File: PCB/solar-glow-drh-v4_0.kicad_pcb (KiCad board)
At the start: 2 copper layers, 50.8 x 88.9 mm, 65 parts, among them J1 UPDI hdr, Q1 BCP5316MTWG, SW2 LED master, U1 AVR64DD28 (VQFN28), U2 ALD910025SALI, U3 ADXL367, U4 TLV3011BIDBVR, U5 NT3H2211, U6 TPS22918

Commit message: pcb(v4_0): stage AEM10300 island parts off-board, net-tagged for rewiring
Place the 13 new v4 harvest parts (U8 AEM10300, U9 LDO, L2, CSRC/CINT/CSTO,
C22-C24, R15-R17, FB1) off the right edge of the board (x>50.8, on B.Cu),
each pad net-tagged per v4-aem10300-prewiring.md section 2, so the ratsnest
guides placement during the rewire. Cloned from existing footprints to match
this board's name-only-net format: U8 from U1 (QFN-28 4x4 0.4mm, 2.65 mm EP
-- matches the AEM10300 land), U9 from U6 (SOT-23), passives from the 0402
land. Larger parts (L2 / CSRC / CINT / CSTO / FB1) are 0402 placeholders to
reland in KiCad.

Existing 65 footprints and all current routing are untouched; the supercap
2S2P pack is verified balanced (VS-[SC1||SC2]-MID-[SC3||SC4]-GND).

Not KiCad-validated (no kicad-cli / pcbnew in this env): open in KiCad to
confirm it loads before relying on it. Structure checked by paren-balance,
reparse (65->78 footprints), and UUID-uniqueness.

Co-Authored-By: Claude Opus 4.8 <noreply@anthropic.com>
Claude-Session: https://claude.ai/code/session_01PBK3zFENdvoGtn8yP7qPA8
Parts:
- added C22: 1uF, solarglow:C1, B.Cu at (57.0, 37.0)
- added C23: 1uF, solarglow:C1, B.Cu at (61.0, 37.0)
- added C24: 100nF, solarglow:C1, B.Cu at (65.0, 37.0)
- added CINT: 10uF *0603, solarglow:C1, B.Cu at (61.0, 32.0)
- added CSRC: 22uF *0805, solarglow:C1, B.Cu at (57.0, 32.0)
- added CSTO: 100uF *bulk, solarglow:C1, B.Cu at (65.0, 32.0)
- added FB1: ferrite *0603, solarglow:C1, B.Cu at (69.0, 37.0)
- added L2: 10uH *IND-land, solarglow:C1, B.Cu at (67.0, 26.0)
- added R15: 2M, solarglow:C1, B.Cu at (57.0, 42.0)
- added R16: 1M, solarglow:C1, B.Cu at (61.0, 42.0)
- added R17: 1M, solarglow:C1, B.Cu at (65.0, 42.0)
- added U8: AEM10300, solarglow:U1, B.Cu at (62.0, 16.0)
- added U9: TPS7A0233 (SOT23-5*), Package_TO_SOT_SMD:SOT-23-6, B.Cu at (58.0, 26.0)

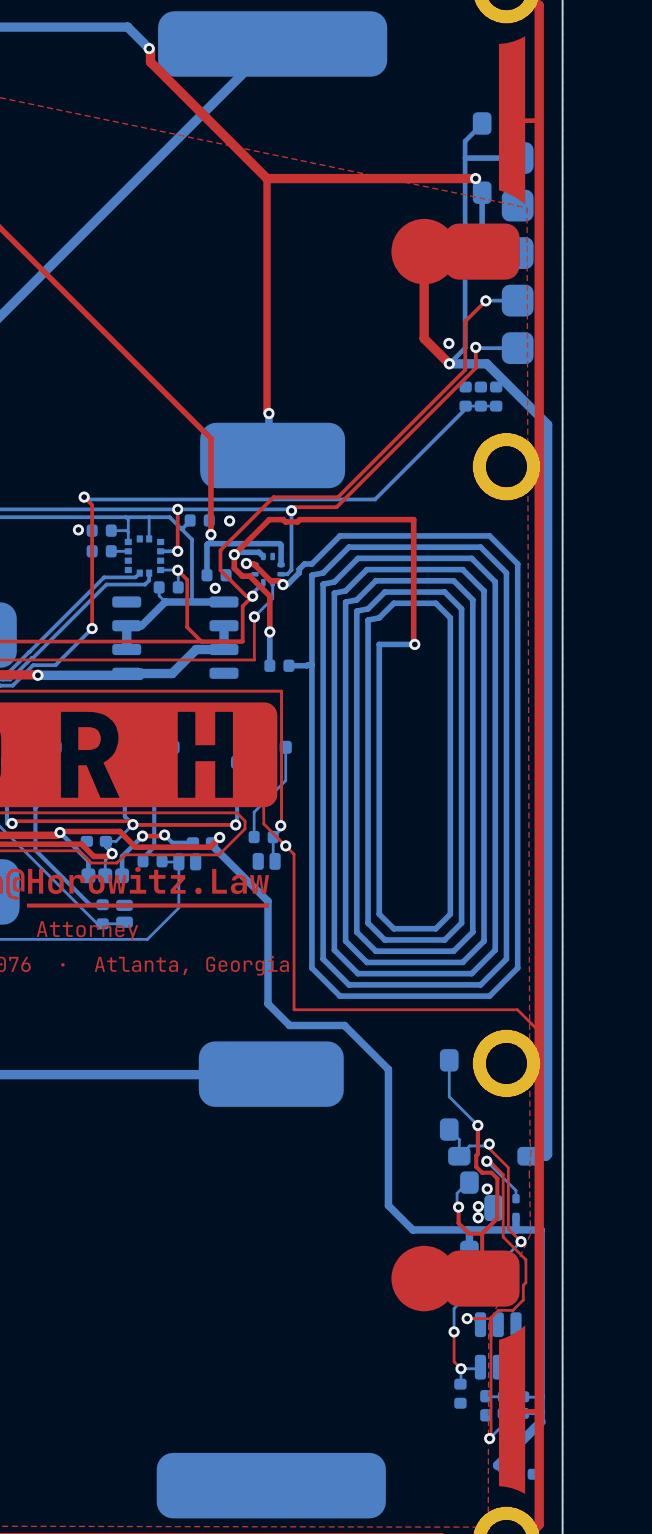
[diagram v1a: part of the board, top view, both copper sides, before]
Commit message: pcb(v4_0): complete v4 netlist -- re-net island endpoints + delete clamp/balancer
Bridge the AEM island into the board (section 3/4 of the pre-wiring plan) so the
ratsnest shows the full v4 wiring task:
- VS -> STO: SC1.P, SC2.P, SW2.1, R12.2, J1.2, JP1.2, TC1.2
- VIN/VINB -> SRC (panels merged): PV1.P/Pt, PV2.P/Pt, R5.1, TP1.1
- MCU spares: U1.PD1 -> STO_SNS, U1.PA4 -> EN_STO_CH

Delete the 11 clamp + balancer parts (section 5): U2, U4, Q1, R7, R8, R9, D10,
D11, C2, D1, D9. Their nets (CLBASE, CLREF, REF_TIE, VCMP, VIN, VINB) vanish.
78 -> 67 footprints.

Only PAD nets change; existing copper/traces are left in place for rip-up during
routing. Self-verified: exact re-net set + counts, vanished nets = 0,
paren-balanced, CRLF preserved, no duplicate UUIDs. Not KiCad-validated (no
kicad-cli here) -- open in KiCad and rip up the old clamp/feed copper as you route.

Co-Authored-By: Claude Opus 4.8 <noreply@anthropic.com>
Claude-Session: https://claude.ai/code/session_01PBK3zFENdvoGtn8yP7qPA8
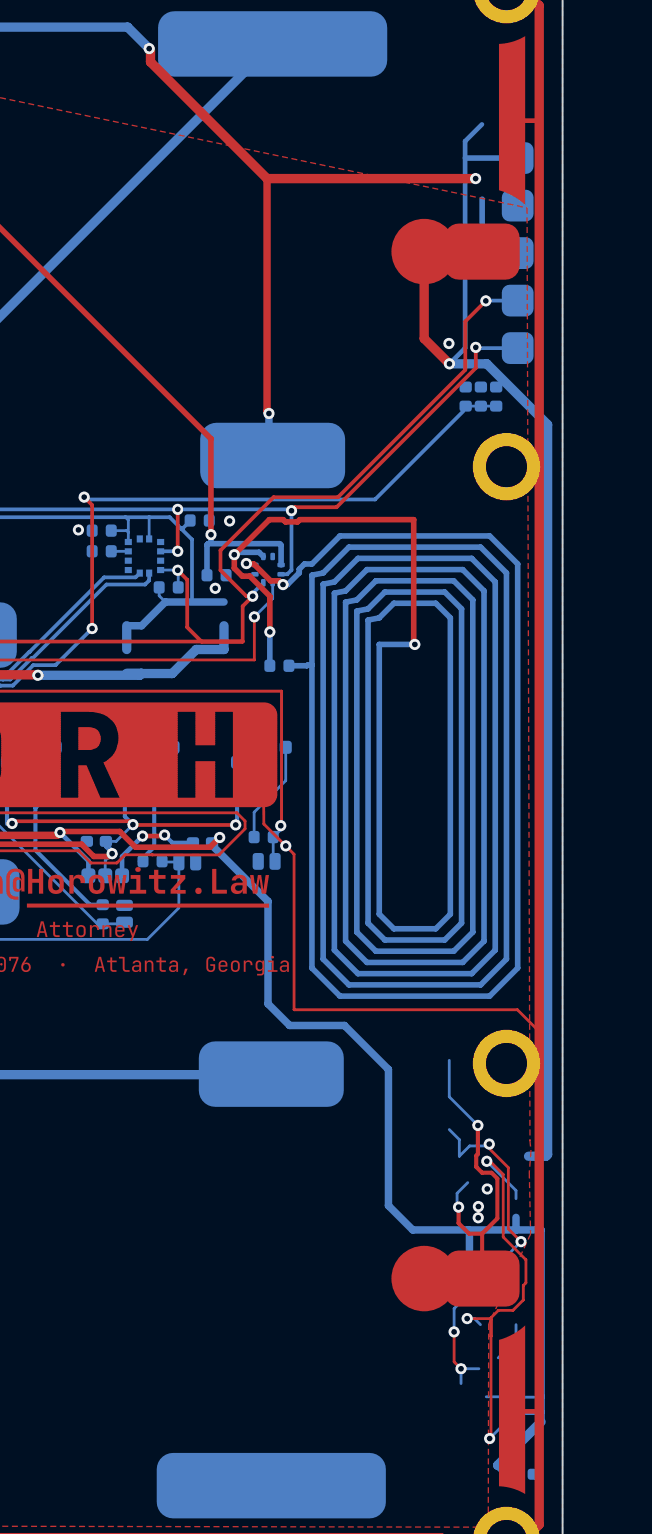
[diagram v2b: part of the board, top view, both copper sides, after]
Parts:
- removed C2: 100nF, solarglow:C2
- removed D1: MMSD301T1G, solarglow:D1
- removed D10: MMSD301T1G, solarglow:D10
- removed D11: MMSD301T1G, solarglow:D11
- removed D9: MMSD301T1G, solarglow:D9
- removed Q1: BCP5316MTWG, solarglow:Q1
- removed R7: 6.81M, solarglow:R7
- removed R8: 3.74M, solarglow:R8
- removed R9: 1k, solarglow:R9
- removed U2: ALD910025SALI, solarglow:U2
- removed U4: TLV3011BIDBVR, Package_TO_SOT_SMD:SOT-23-6
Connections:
- J1 pad 2: VS -> STO
- JP1 pad 2: VS -> STO
- PV1 pad P: VIN -> SRC
- PV1 pad Pt: VIN -> SRC
- PV2 pad P: VINB -> SRC
- PV2 pad Pt: VINB -> SRC
- R12 pad 2: VS -> STO
- R5 pad 1: VIN -> SRC
- SC1 pad P: VS -> STO
- SC2 pad P: VS -> STO
- SW2 pad 1: VS -> STO
- TC1 pad 2: VS -> STO
- TP1 pad 1: VIN -> SRC
- U1 pad 11: unconnected-(U1-PD1-Pad11) -> STO_SNS
- U1 pad 2: PA4 -> EN_STO_CH
